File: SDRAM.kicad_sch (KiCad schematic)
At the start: 13 parts, among them U1 IS42S32800J-6TL

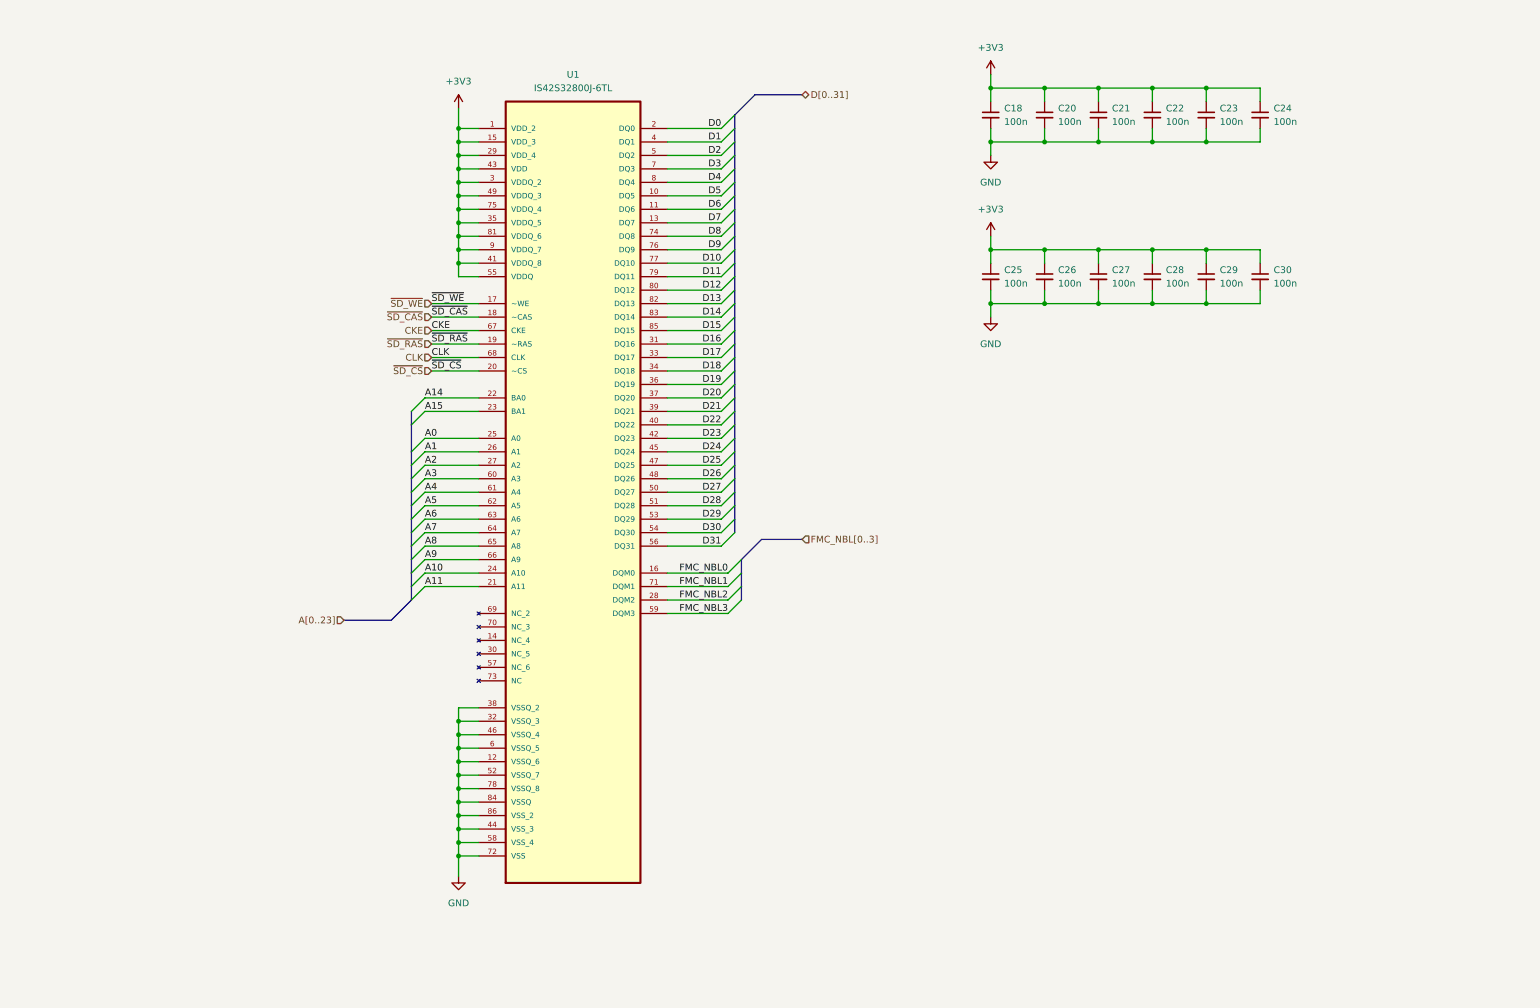
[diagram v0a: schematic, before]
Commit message: Added UART, i2c, debug, NAND Flash, NOR Flash, EEPROM, SD-Card
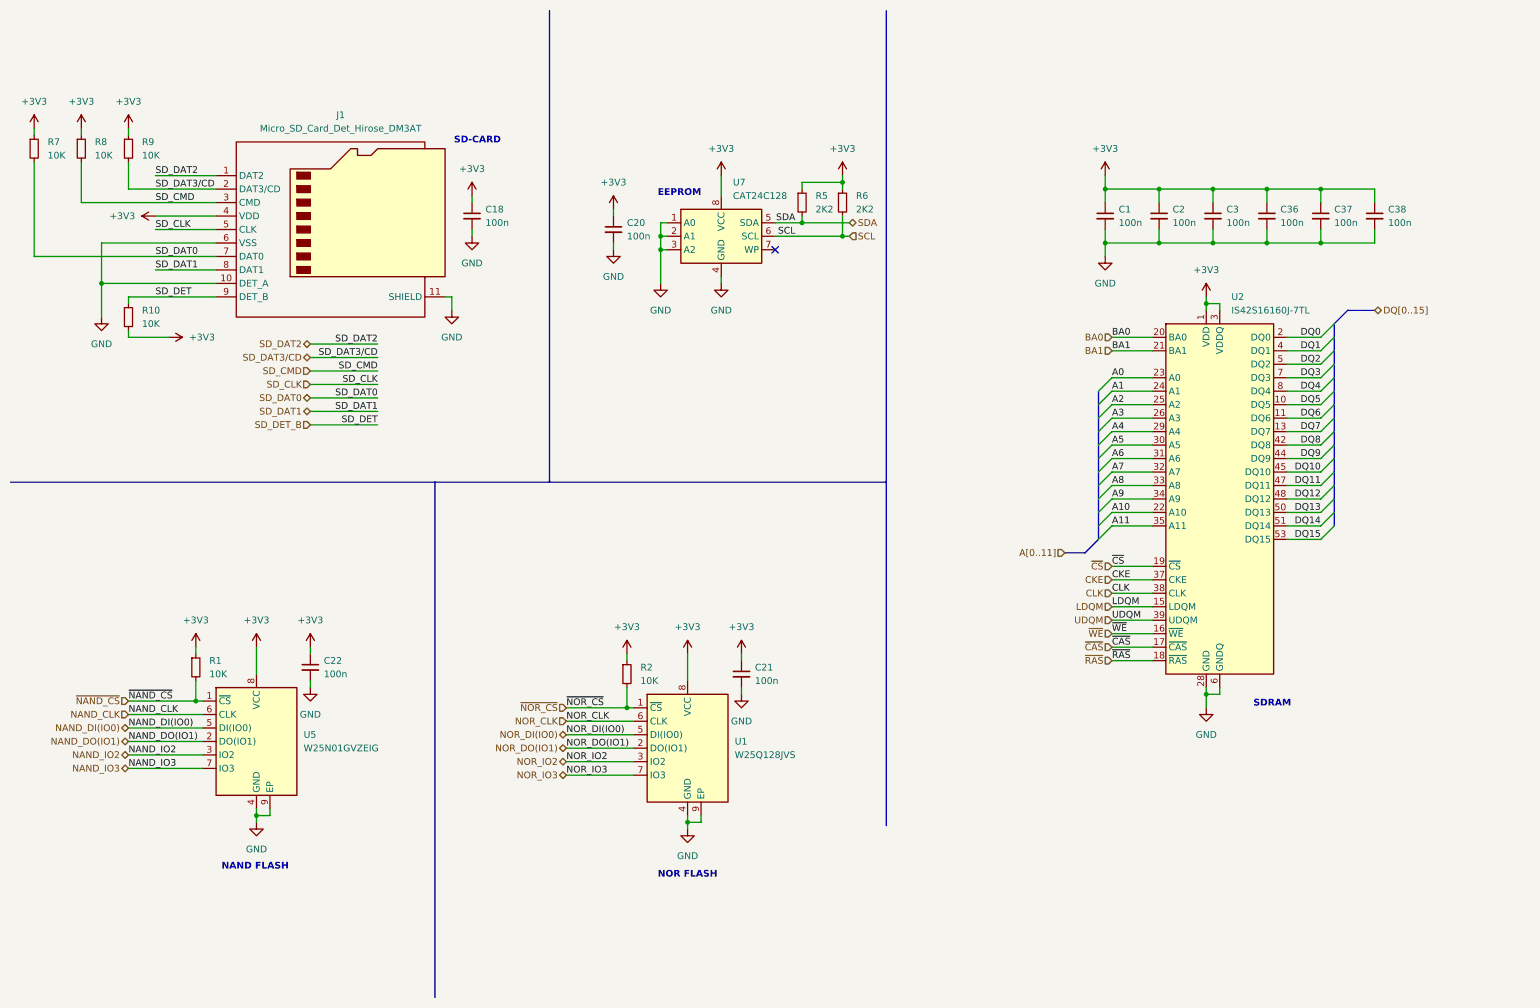
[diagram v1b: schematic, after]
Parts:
- removed C23, C24, C25, C26, C27, C28, C29, C30: 100n, Capacitor_SMD:C_0201_0603Metric, symbol Device:C_Small
- removed U1: IS42S32800J-6TL, IS42S32800J-6TL:SOP50P1176X120-86N, symbol IS42S32800J-6TL:IS42S32800J-6TL
- added C1, C2, C3, C36, C37, C38: 100n, Capacitor_SMD:C_0402_1005Metric, symbol Device:C_Small
- added J1: Micro_SD_Card_Det_Hirose_DM3AT, Connector_Card:microSD_HC_Hirose_DM3AT-SF-PEJM5, symbol Connector:Micro_SD_Card_Det_Hirose_DM3AT
- added R1, R10, R2, R7, R8, R9: 10K, Resistor_SMD:R_0402_1005Metric, symbol Device:R_Small
- added R5, R6: 2K2, Resistor_SMD:R_0402_1005Metric, symbol Device:R_Small
- added U1: W25Q128JVS, Package_SON:WSON-8-1EP_6x5mm_P1.27mm_EP3.4x4.3mm, symbol Memory_Flash:W25Q32JVZP
- added U2: IS42S16160J-7TL, Package_SO:TSOP-II-54_22.2x10.16mm_P0.8mm, symbol Memory_RAM:IS42S16400J-xC
- added U5: W25N01GVZEIG, Package_SON:WSON-8-1EP_6x5mm_P1.27mm_EP3.4x4.3mm, symbol Memory_Flash:W25Q32JVZP
- added U7: CAT24C128, Package_SO:SOIC-8_3.9x4.9mm_P1.27mm, symbol Memory_EEPROM:CAT24C128
- C18, C20, C21, C22: footprint Capacitor_SMD:C_0201_0603Metric -> Capacitor_SMD:C_0402_1005Metric
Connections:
- net +3V3: now also C1.1, C2.1, C3.1, C36.1, C37.1, C38.1, J1.4 (VDD), R1.1, R10.2, R2.1, R5.1, R6.1, R7.1, R8.1, R9.1, U1.8 (VCC), U2.1 (VDD), U2.14 (VDD), U2.27 (VDD), U2.3 (VDDQ), U2.43 (VDDQ), U2.49 (VDDQ), U2.9 (VDDQ), U5.8 (VCC), U7.8 (VCC)
- net A0: now also U2.23 (A0)
- net A1: now also U2.24 (A1)
- net A10: now also U2.22 (A10)
- net A11: now also U2.35 (A11)
- net A2: now also U2.25 (A2)
- net A3: now also U2.26 (A3)
- net A4: now also U2.29 (A4)
- net A5: now also U2.30 (A5)
- net A6: now also U2.31 (A6)
- net A7: now also U2.32 (A7)
- net A8: now also U2.33 (A8)
- net A9: now also U2.34 (A9)
- net CKE: now also U2.37 (CKE)
- net CLK: now also U2.38 (CLK)
- net GND: now also C1.2, C2.2, C3.2, C36.2, C37.2, C38.2, J1.10 (DET_A), J1.11 (SHIELD), J1.6 (VSS), U1.4 (GND), U1.9 (EP), U2.12 (GNDQ), U2.28 (GND), U2.41 (GND), U2.46 (GNDQ), U2.52 (GNDQ), U2.54 (GND), U2.6 (GNDQ), U5.4 (GND), U5.9 (EP), U7.1 (A0), U7.2 (A1), U7.3 (A2), U7.4 (GND)
- new net BA0: U2.20 (BA0)
- new net BA1: U2.21 (BA1)
- new net DQ0: U2.2 (DQ0)
- new net DQ1: U2.4 (DQ1)
- new net DQ10: U2.45 (DQ10)
- new net DQ11: U2.47 (DQ11)
- new net DQ12: U2.48 (DQ12)
- new net DQ13: U2.50 (DQ13)
- new net DQ14: U2.51 (DQ14)
- new net DQ15: U2.53 (DQ15)
- new net DQ2: U2.5 (DQ2)
- new net DQ3: U2.7 (DQ3)
- new net DQ4: U2.8 (DQ4)
- new net DQ5: U2.10 (DQ5)
- new net DQ6: U2.11 (DQ6)
- new net DQ7: U2.13 (DQ7)
- new net DQ8: U2.42 (DQ8)
- new net DQ9: U2.44 (DQ9)
- new net LDQM: U2.15 (LDQM)
- new net NAND_CLK: U5.6 (CLK)
- new net NAND_DI(IO0): U5.5 (DI(IO0))
- new net NAND_DO(IO1): U5.2 (DO(IO1))
- new net NAND_IO2: U5.3 (IO2)
- new net NAND_IO3: U5.7 (IO3)
- new net NOR_CLK: U1.6 (CLK)
- new net NOR_DI(IO0): U1.5 (DI(IO0))
- new net NOR_DO(IO1): U1.2 (DO(IO1))
- new net NOR_IO2: U1.3 (IO2)
- new net NOR_IO3: U1.7 (IO3)
- new net SCL: R6.2, U7.6 (SCL)
- new net SDA: R5.2, U7.5 (SDA)
- new net SD_CLK: J1.5 (CLK)
- new net SD_CMD: J1.3 (CMD), R8.2
- new net SD_DAT0: J1.7 (DAT0), R7.2
- new net SD_DAT1: J1.8 (DAT1)
- new net SD_DAT2: J1.1 (DAT2)
- new net SD_DAT3/CD: J1.2 (DAT3/CD), R9.2
- new net SD_DET_B: J1.9 (DET_B), R10.1
- new net UDQM: U2.39 (UDQM)
- new net ~{CAS}: U2.17 (~{CAS})
- new net ~{CS}: U2.19 (~{CS})
- new net ~{NAND_CS}: R1.2, U5.1 (~{CS})
- new net ~{NOR_CS}: R2.2, U1.1 (~{CS})
- new net ~{RAS}: U2.18 (~{RAS})
- new net ~{WE}: U2.16 (~{WE})
- no-connect marks 0 -> 1
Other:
- note added: "EEPROM"
- note added: "NAND FLASH"
- note added: "NOR FLASH"
- note added: "SD-CARD"
- note added: "SDRAM"

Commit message: Added I2S Audio amplifier
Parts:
- C1, C18, C2, C20, C21, C22, C3, C36, C37, C38: footprint Capacitor_SMD:C_0402_1005Metric -> Capacitor_SMD:C_0201_0603Metric
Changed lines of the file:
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@@
 			)
 		)
-		(property "Footprint" "Capacitor_SMD:C_0402_1005Metric"
+		(property "Footprint" "Capacitor_SMD:C_0201_0603Metric"
 			(at 238.76 50.8 0)
 			(effects
@@
 			)
 		)
-		(property "Footprint" "Capacitor_SMD:C_0402_1005Metric"
+		(property "Footprint" "Capacitor_SMD:C_0201_0603Metric"
 			(at 99.06 50.8 0)
 			(effects
@@
 			)
 		)
-		(property "Footprint" "Capacitor_SMD:C_0402_1005Metric"
+		(property "Footprint" "Capacitor_SMD:C_0201_0603Metric"
 			(at 259.08 50.8 0)
 			(effects
@@
 			)
 		)
-		(property "Footprint" "Capacitor_SMD:C_0402_1005Metric"
+		(property "Footprint" "Capacitor_SMD:C_0201_0603Metric"
 			(at 149.86 137.16 0)
 			(effects
@@
 			)
 		)
-		(property "Footprint" "Capacitor_SMD:C_0402_1005Metric"
+		(property "Footprint" "Capacitor_SMD:C_0201_0603Metric"
 			(at 269.24 50.8 0)
 			(effects
@@
 			)
 		)
-		(property "Footprint" "Capacitor_SMD:C_0402_1005Metric"
+		(property "Footprint" "Capacitor_SMD:C_0201_0603Metric"
 			(at 125.73 53.34 0)
 			(effects
@@
 			)
 		)
-		(property "Footprint" "Capacitor_SMD:C_0402_1005Metric"
+		(property "Footprint" "Capacitor_SMD:C_0201_0603Metric"
 			(at 228.6 50.8 0)
 			(effects
@@
 			)
 		)
-		(property "Footprint" "Capacitor_SMD:C_0402_1005Metric"
+		(property "Footprint" "Capacitor_SMD:C_0201_0603Metric"
 			(at 248.92 50.8 0)
 			(effects
@@
 			)
 		)
-		(property "Footprint" "Capacitor_SMD:C_0402_1005Metric"
+		(property "Footprint" "Capacitor_SMD:C_0201_0603Metric"
 			(at 68.58 135.89 0)
 			(effects
@@
 			)
 		)
-		(property "Footprint" "Capacitor_SMD:C_0402_1005Metric"
+		(property "Footprint" "Capacitor_SMD:C_0201_0603Metric"
 			(at 218.44 50.8 0)
 			(effects

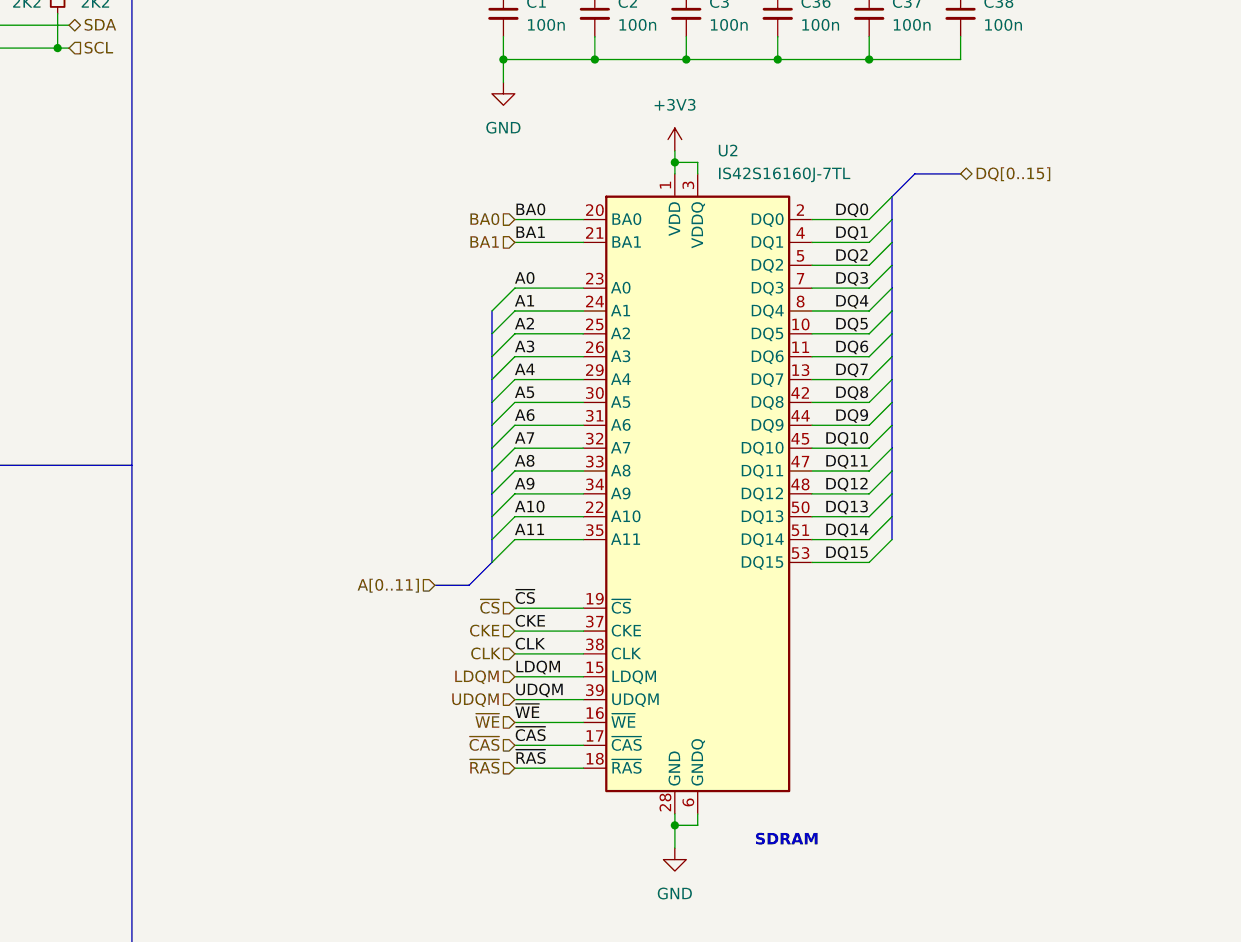
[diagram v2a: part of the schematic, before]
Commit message: Finish high speed sdram tracks
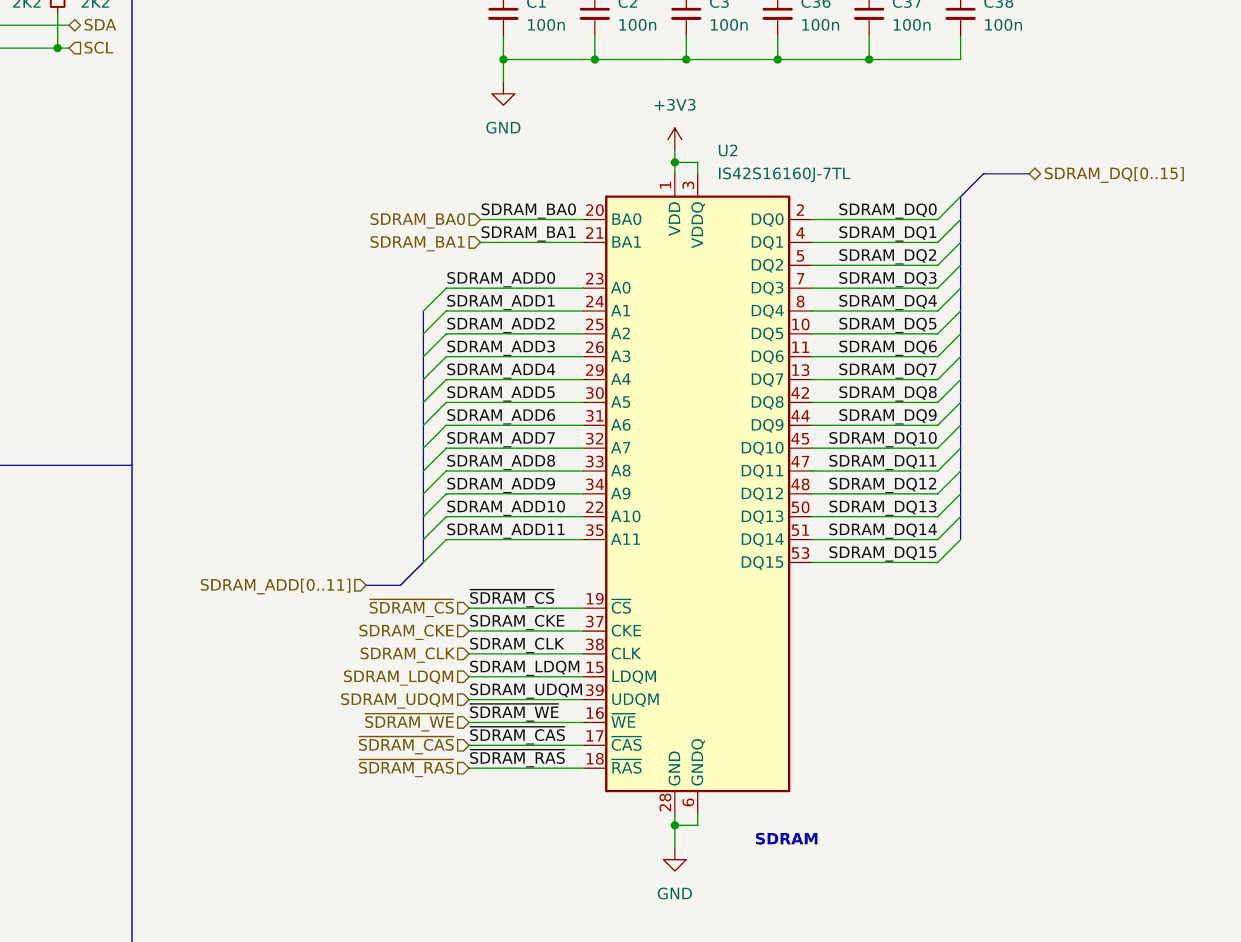
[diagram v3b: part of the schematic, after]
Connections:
- net A0 renamed SDRAM_ADD0
- net A1 renamed SDRAM_ADD1
- net A10 renamed SDRAM_ADD10
- net A11 renamed SDRAM_ADD11
- net A2 renamed SDRAM_ADD2
- net A3 renamed SDRAM_ADD3
- net A4 renamed SDRAM_ADD4
- net A5 renamed SDRAM_ADD5
- net A6 renamed SDRAM_ADD6
- net A7 renamed SDRAM_ADD7
- net A8 renamed SDRAM_ADD8
- net A9 renamed SDRAM_ADD9
- net BA0 renamed SDRAM_BA0
- net BA1 renamed SDRAM_BA1
- net CKE renamed SDRAM_CKE
- net CLK renamed SDRAM_CLK
- net DQ0 renamed SDRAM_DQ0
- net DQ1 renamed SDRAM_DQ1
- net DQ10 renamed SDRAM_DQ10
- net DQ11 renamed SDRAM_DQ11
- net DQ12 renamed SDRAM_DQ12
- net DQ13 renamed SDRAM_DQ13
- net DQ14 renamed SDRAM_DQ14
- net DQ15 renamed SDRAM_DQ15
- net DQ2 renamed SDRAM_DQ2
- net DQ3 renamed SDRAM_DQ3
- net DQ4 renamed SDRAM_DQ4
- net DQ5 renamed SDRAM_DQ5
- net DQ6 renamed SDRAM_DQ6
- net DQ7 renamed SDRAM_DQ7
- net DQ8 renamed SDRAM_DQ8
- net DQ9 renamed SDRAM_DQ9
- net LDQM renamed SDRAM_LDQM
- net UDQM renamed SDRAM_UDQM
- net ~{CAS} renamed ~{SDRAM_CAS}
- net ~{CS} renamed ~{SDRAM_CS}
- net ~{RAS} renamed ~{SDRAM_RAS}
- net ~{WE} renamed ~{SDRAM_WE}

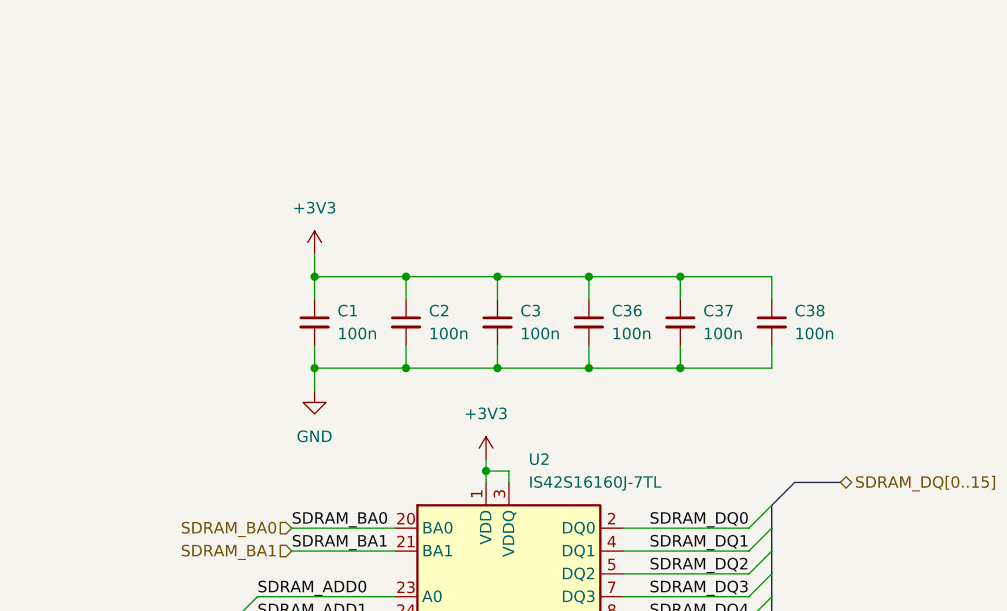
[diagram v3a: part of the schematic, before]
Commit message: Finish sdram, LCD, SD-card, QSPI, I2S tracks
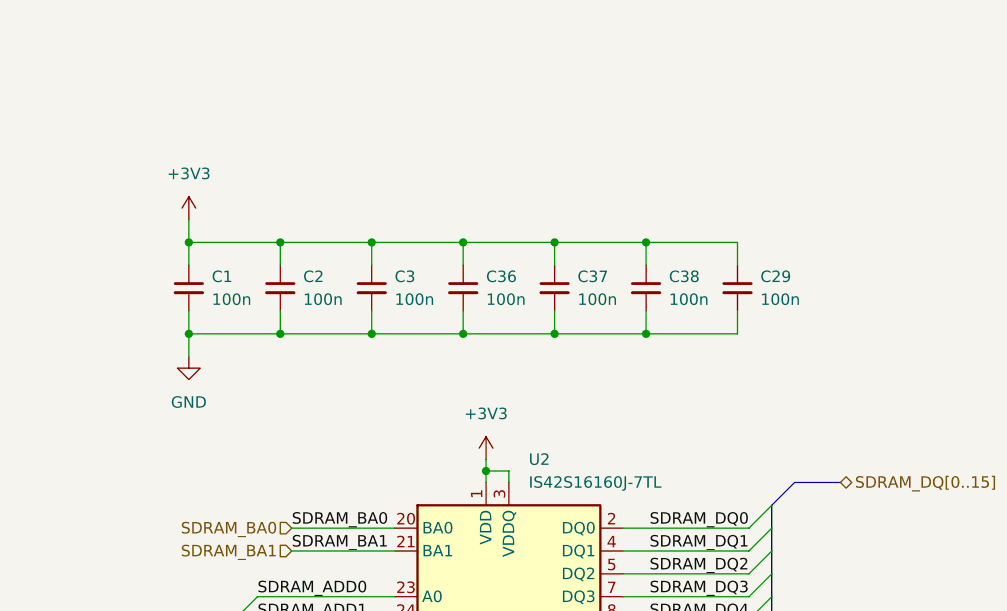
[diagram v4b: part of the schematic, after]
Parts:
- added C29: 100n, Capacitor_SMD:C_0402_1005Metric, symbol Device:C_Small
- C1, C18, C2, C20, C21, C22, C3, C36, C37, C38: footprint Capacitor_SMD:C_0201_0603Metric -> Capacitor_SMD:C_0402_1005Metric
- U1: footprint Package_SON:WSON-8-1EP_6x5mm_P1.27mm_EP3.4x4.3mm -> Package_SON:WSON-8-1EP_8x6mm_P1.27mm_EP3.4x4.3mm
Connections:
- net +3V3: now also C29.1
- net GND: now also C29.2
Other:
- moved on the sheet: C1, C2, C3, C36, C37, C38
